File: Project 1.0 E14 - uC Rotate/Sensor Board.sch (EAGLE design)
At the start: 97 parts, among them IC1 LT1963EST-1.5, IC2 LT1963EST-1.5, IC4 LT1963EST-1.5

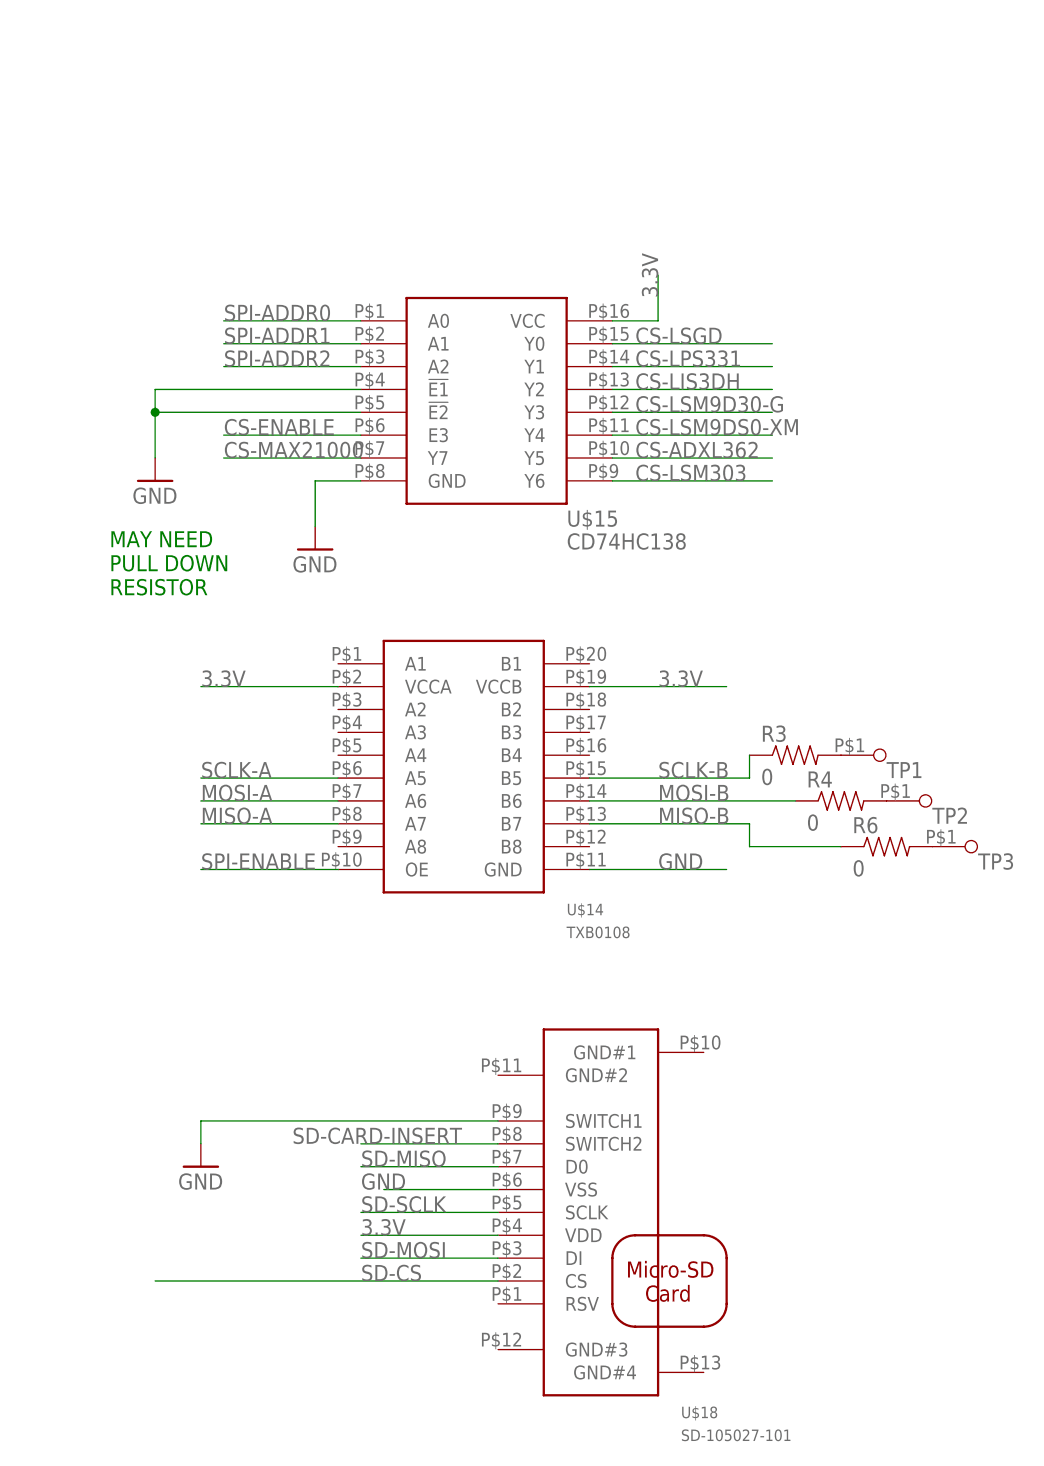
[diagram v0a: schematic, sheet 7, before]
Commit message: Sensor Board: Chnaged 3:8 mux for a 4:10 mux and removed traces that were no longer valid, rerouting is now needed
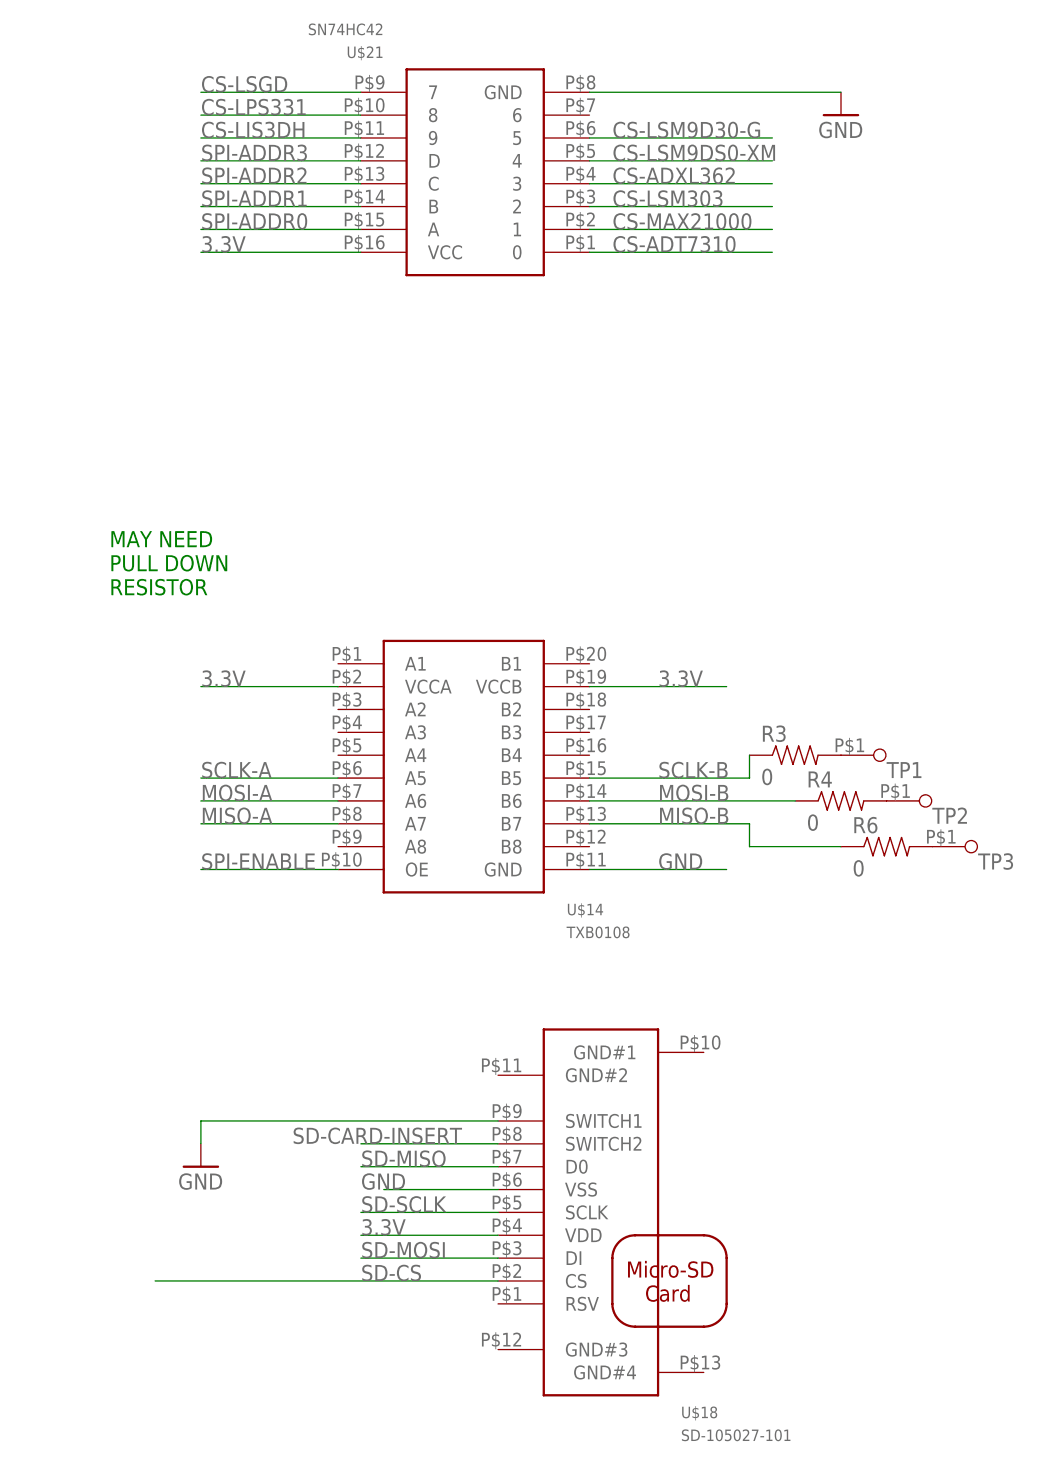
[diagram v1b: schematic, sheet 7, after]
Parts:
- removed U$15: CD74HC138, Kas-Buffers & Level Shifters:CD74HC138
- added U$21: SN74HC42, Kas-Buffers & Level Shifters:SN74HC42
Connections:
- removed net CS-ENABLE: U$11.PA0, U$15.E3
- new net INT2-H3LIS331: U$11.PD7, U$2.INT2
- new net SPI-ADDR3: U$11.PA3, U$21.D
- net 3.3V: now also U$21.VCC; no longer U$15.VCC
- net CS-ADT7310: now also U$21.0; no longer U$11.PD4
- net CS-ADXL362: now also U$21.3; no longer U$15.Y5
- net CS-H3LIS331DLTR: no longer U$11.PD7
- net CS-LIS3DH: now also U$21.9; no longer U$15.Y2
- net CS-LPS331: now also U$21.8; no longer U$15.Y1
- net CS-LSGD: now also U$21.7; no longer U$15.Y0
- net CS-LSM303: now also U$21.2; no longer U$15.Y6
- net CS-LSM9D30-G: now also U$21.5; no longer U$15.Y3
- net CS-LSM9DS0-XM: now also U$21.4; no longer U$15.Y4
- net CS-MAX21000: now also U$21.1; no longer U$15.Y7
- net GND: now also U$21.GND; no longer U$15.!E1, U$15.!E2, U$15.GND
- net SPI-ADDR0: now also U$11.PA0, U$21.A; no longer U$11.PA3, U$15.A0
- net SPI-ADDR1: now also U$11.PA1, U$21.B; no longer U$11.PA2, U$15.A1
- net SPI-ADDR2: now also U$11.PA2, U$21.C; no longer U$11.PA1, U$15.A2

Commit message: Sensor Test Board: Changed tmperature sensor for ADT7301 using a smaller package (SOT32-6). Reconnected CS traces in a organised fasion. Hid Power and GND traces.
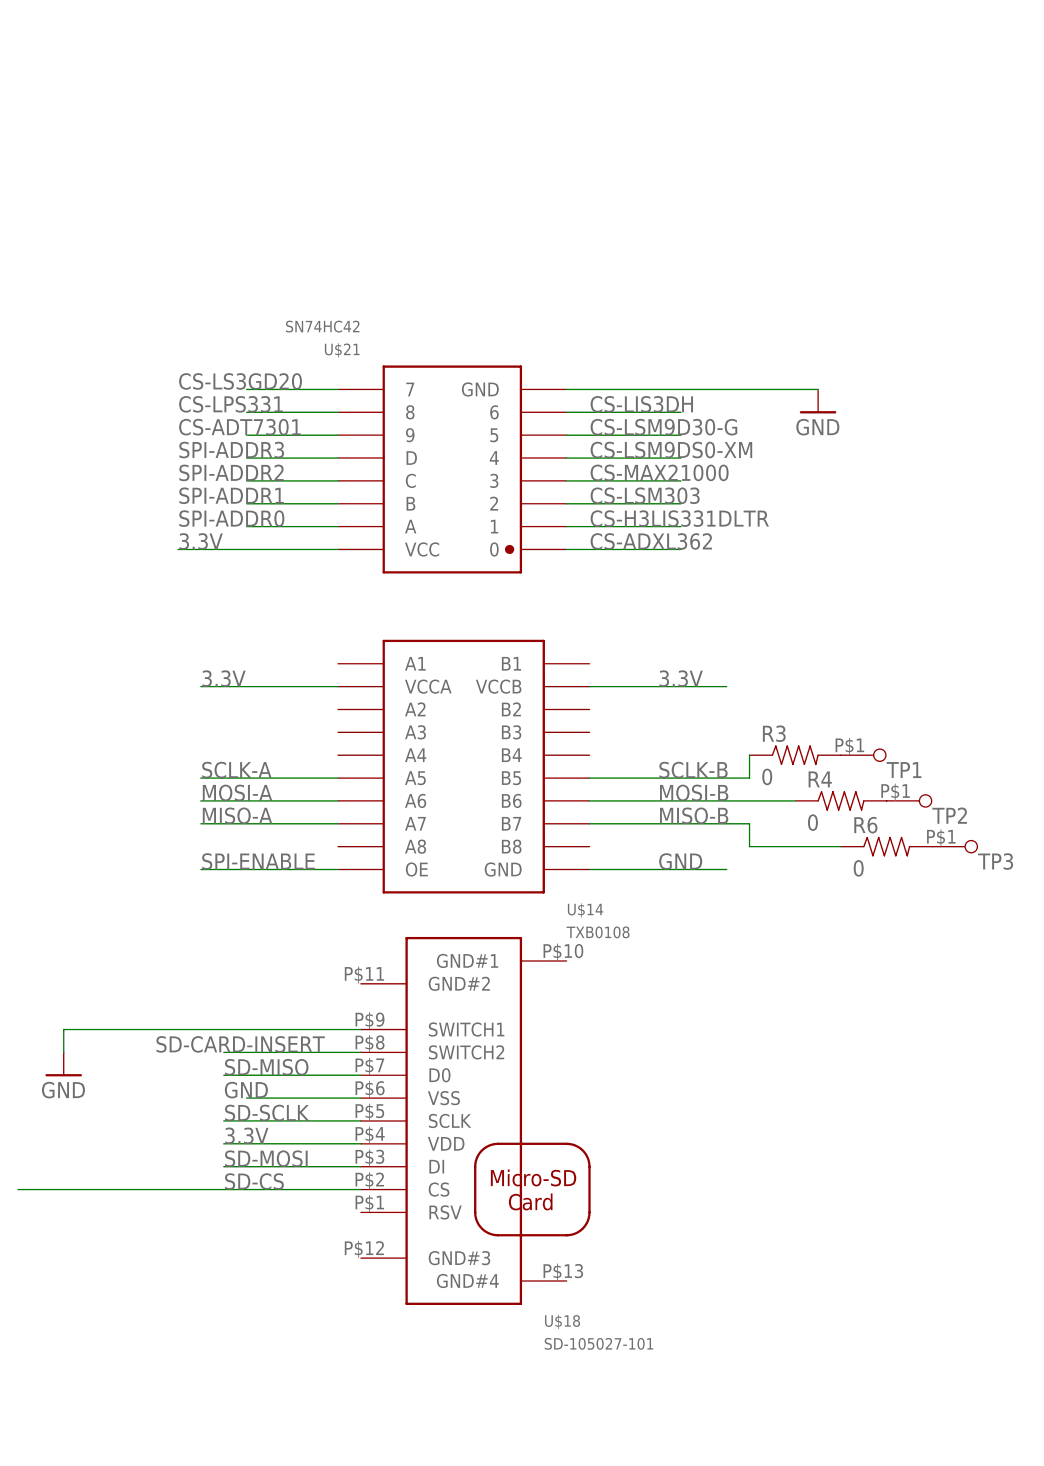
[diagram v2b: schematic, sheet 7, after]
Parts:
- removed C22: 0.1uF, Kas-Passives:CAPACITOR
- removed R8, R9: 10k, Kas-Passives:RESISTOR
- removed U$7: ADT7310, Kas-Sensors:ADT7310
- added C52: 0.1uF, Kas-Passives:CAPACITOR
- added U$15: ADT7301, Kas-Sensors:ADT7301
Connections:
- net CS-LSGD renamed CS-LS3GD20
- removed net CS-ADT7310: U$21.0, U$7.!CS
- removed net CT-ADT7310: R8.1, U$7.CT
- removed net INT-ADT7310: R9.1, U$7.INT
- new net CS-ADT7301: U$15.!CS, U$21.9
- new net N$2: C52.1, U$15.VDD
- net 3.3V: no longer C22.1, R8.2, R9.2, U$7.VDD
- net CS-ADXL362: now also U$21.0; no longer U$21.3
- net CS-H3LIS331DLTR: now also U$21.1
- net CS-LIS3DH: now also U$21.6; no longer U$21.9
- net CS-MAX21000: now also U$21.3; no longer U$21.1
- net GND: now also C52.2, U$15.GND; no longer C22.2, U$7.GND
- net MISO-B: now also U$15.DOUT; no longer U$7.DOUT
- net MOSI-B: now also U$15.DIN; no longer U$7.DIN
- net SCLK-B: now also U$15.SCLK; no longer U$7.SCLK
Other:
- note removed: "MAY NEED PULL DOWN RESISTOR"
- moved on the sheet: U$18

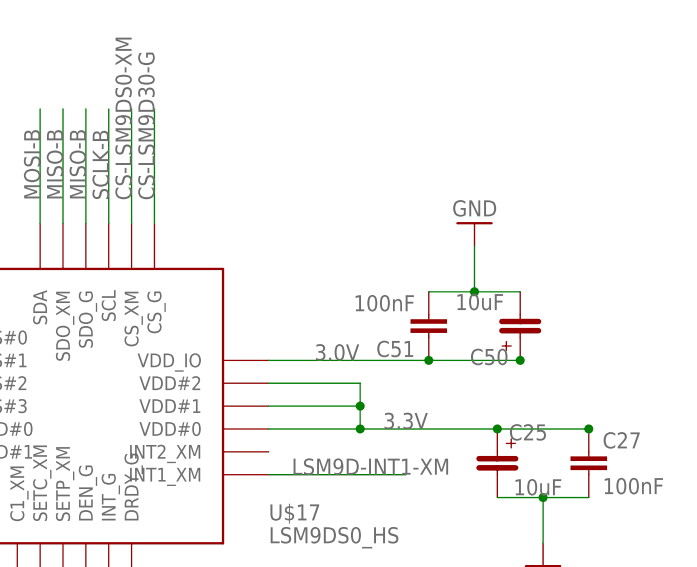
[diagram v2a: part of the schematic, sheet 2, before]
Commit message: Sensor Test Board: Swapped order of magnotometers, reorganised CS traces to prevent overlaps and connected new teperature sensor. Removed LS9D Vio bulk and decoupling capacitors. SPI test points were disconected but not removed. SPI vertical traces were spaced correctly with a minimum of 6x trace with spacing between traces.
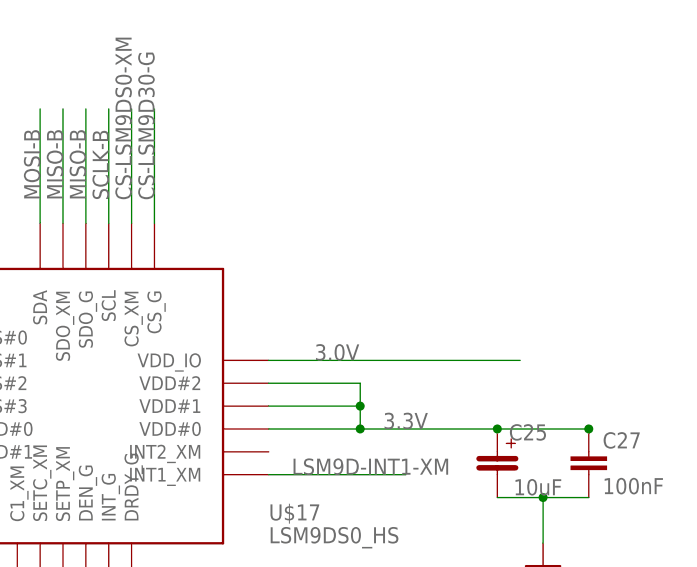
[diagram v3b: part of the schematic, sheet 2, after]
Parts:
- removed C50: 10uF, Kas-Passives:EEFCD0J100ER
- removed C51: 100nF, Kas-Passives:CAPACITOR
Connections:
- net 3.0V: no longer C50.@P$1, C51.1
- net CS-LSM303: now also U$21.5; no longer U$21.2
- net CS-LSM9D30-G: now also U$21.3; no longer U$21.5
- net CS-LSM9DS0-XM: now also U$21.2; no longer U$21.4
- net CS-MAX21000: now also U$21.4; no longer U$21.3
- net GND: no longer C50.@P$2, C51.2
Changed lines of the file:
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@@
 <part name="GND43" library="SparkFun-Aesthetics" deviceset="GND" device=""/>
 <part name="GND44" library="SparkFun-Aesthetics" deviceset="GND" device=""/>
-<part name="C50" library="Kas-Passives" deviceset="EEFCD0J100ER" device="" value="10uF"/>
-<part name="C51" library="Kas-Passives" deviceset="CAPACITOR" device="" value="100nF"/>
-<part name="GND45" library="SparkFun-Aesthetics" deviceset="GND" device=""/>
 <part name="R7" library="Kas-Passives" deviceset="RESISTOR" device="" value="10k"/>
 <part name="U$18" library="Kas-Connectors" deviceset="SD-105027-101" device=""/>
@@
 <instance part="GND43" gate="1" x="-17.78" y="-35.56"/>
 <instance part="GND44" gate="1" x="50.8" y="-17.78"/>
-<instance part="C50" gate="G$1" x="48.26" y="5.08" rot="R90"/>
-<instance part="C51" gate="G$1" x="38.1" y="10.16" rot="R180"/>
-<instance part="GND45" gate="1" x="43.18" y="20.32" rot="R180"/>
 <instance part="U$2" gate="G$1" x="5.08" y="-132.08"/>
 <instance part="GND8" gate="1" x="45.72" y="-132.08"/>
@@
 </segment>
 <segment>
-<pinref part="C50" gate="G$1" pin="@P$2"/>
-<pinref part="C51" gate="G$1" pin="2"/>
-<wire x1="48.26" y1="12.7" x2="43.18" y2="12.7" width="0.1524" layer="91"/>
-<wire x1="43.18" y1="12.7" x2="38.1" y2="12.7" width="0.1524" layer="91"/>
-<wire x1="43.18" y1="12.7" x2="43.18" y2="17.78" width="0.1524" layer="91"/>
-<junction x="43.18" y="12.7"/>
-<pinref part="GND45" gate="1" pin="GND"/>
-</segment>
-<segment>
 <pinref part="U$2" gate="G$1" pin="GND#1"/>
 <wire x1="25.4" y1="-127" x2="45.72" y2="-127" width="0.1524" layer="91"/>
@@
 <net name="3.0V" class="0">
 <segment>
-<pinref part="C50" gate="G$1" pin="@P$1"/>
-<wire x1="48.26" y1="5.08" x2="38.1" y2="5.08" width="0.1524" layer="91"/>
-<junction x="48.26" y="5.08"/>
-<pinref part="C51" gate="G$1" pin="1"/>
-<junction x="38.1" y="5.08"/>
 <pinref part="U$17" gate="G$1" pin="VDD_IO"/>
-<wire x1="20.32" y1="5.08" x2="38.1" y2="5.08" width="0.1524" layer="91"/>
+<wire x1="20.32" y1="5.08" x2="48.26" y2="5.08" width="0.1524" layer="91"/>
 <label x="25.4" y="5.08" size="1.778" layer="95"/>
 </segment>
@@
 <net name="CS-LSM303" class="0">
 <segment>
+<label x="15.24" y="27.94" size="1.778" layer="95"/>
+<pinref part="U$21" gate="G$1" pin="5"/>
+<wire x1="12.7" y1="35.56" x2="25.4" y2="35.56" width="0.1524" layer="91"/>
+</segment>
+</net>
+<net name="CS-MAX21000" class="0">
+<segment>
+<label x="15.24" y="30.48" size="1.778" layer="95"/>
+<pinref part="U$21" gate="G$1" pin="4"/>
+<wire x1="12.7" y1="33.02" x2="25.4" y2="33.02" width="0.1524" layer="91"/>
+</segment>
+</net>
+<net name="CS-LSM9DS0-XM" class="0">
+<segment>
+<label x="15.24" y="33.02" size="1.778" layer="95"/>
 <pinref part="U$21" gate="G$1" pin="2"/>
 <wire x1="12.7" y1="27.94" x2="25.4" y2="27.94" width="0.1524" layer="91"/>
-<label x="15.24" y="27.94" size="1.778" layer="95"/>
-</segment>
-</net>
-<net name="CS-MAX21000" class="0">
-<segment>
+</segment>
+</net>
+<net name="CS-LSM9D30-G" class="0">
+<segment>
+<label x="15.24" y="35.56" size="1.778" layer="95"/>
 <pinref part="U$21" gate="G$1" pin="3"/>
 <wire x1="12.7" y1="30.48" x2="25.4" y2="30.48" width="0.1524" layer="91"/>
-<label x="15.24" y="30.48" size="1.778" layer="95"/>
-</segment>
-</net>
-<net name="CS-LSM9DS0-XM" class="0">
-<segment>
-<pinref part="U$21" gate="G$1" pin="4"/>
-<wire x1="12.7" y1="33.02" x2="25.4" y2="33.02" width="0.1524" layer="91"/>
-<label x="15.24" y="33.02" size="1.778" layer="95"/>
-</segment>
-</net>
-<net name="CS-LSM9D30-G" class="0">
-<segment>
-<pinref part="U$21" gate="G$1" pin="5"/>
-<wire x1="12.7" y1="35.56" x2="25.4" y2="35.56" width="0.1524" layer="91"/>
-<label x="15.24" y="35.56" size="1.778" layer="95"/>
-</segment>
-</net>
+</segment>
+</net>
